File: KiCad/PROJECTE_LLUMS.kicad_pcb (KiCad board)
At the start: 2 copper layers, 82.8 x 63 mm, 60 parts, among them J1 CONNECTOR_MOTOR, J2 Conn_01x03, J3 Conn_01x03, Q2 IRLZ44N, Q3 IRLZ44N, Q4 IRLZ44N, Q5 IRLZ44N, Q6 IRLZ44N, Q7 IRLZ44N, SW1 SW_Push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

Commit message: routing
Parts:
- added C10: 10uF, Capacitor_SMD:C_0805_2012Metric_Pad1.18x1.45mm_HandSolder, F.Cu at (92.6, 109.4)
- added C11: 10uF, Capacitor_SMD:C_0805_2012Metric_Pad1.18x1.45mm_HandSolder, F.Cu at (89.7, 109.3)
- added J4: Conn_01x02_Pin, TerminalBlock:TerminalBlock_MaiXu_MX126-5.0-02P_1x02_P5.00mm, F.Cu at (102.5, 76.9)
- moved D6 311.5 mm to (240.8, 80.9), turned to 180 degrees
- moved D5 307.6 mm to (240.8, 88.3), turned to 180 degrees
- moved D4 304.3 mm to (240.8, 95.8), turned to 180 degrees
- moved D3 301.8 mm to (240.8, 103.3), turned to 180 degrees
- moved D2 300.0 mm to (240.8, 110.7), turned to 180 degrees
- moved Q7 295.7 mm to (232.6, 80.8), turned to 180 degrees
- moved R2 294.1 mm to (238.5, 120.2), turned to 180 degrees
- moved Q6 292.4 mm to (232.6, 86.8), turned to 180 degrees
- moved Q5 289.5 mm to (232.6, 92.7), turned to 180 degrees
- moved Q4 287.0 mm to (232.6, 98.7), turned to 180 degrees
- moved Q3 285.1 mm to (232.6, 104.6), turned to 180 degrees
- moved Q2 283.6 mm to (232.6, 110.5), turned to 180 degrees
- moved R3 275.0 mm to (229.0, 120.2), turned to 180 degrees
- moved J1 262.4 mm to (220.8, 103.0), turned to 180 degrees
- moved D7 262.2 mm to (221.9, 111.1), turned to 180 degrees
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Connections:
- net 12V renamed /alimentacio/12V
- net Net-(D8-A) renamed /alimentacio/OUT
- net Net-(J3-Pin_1) renamed /Debug/CON1
- net Net-(J3-Pin_2) renamed /Debug/CON2
- net Net-(U7-OSC1/CLKI/CN30/RA2) renamed /microcontrolador/OSC1
- net Net-(U7-OSC2/CLKO/CN29/PMA0/RA3) renamed /microcontrolador/OSC2
- net Net-(U7-VCAP) renamed /microcontrolador/VCAP
- net Net-(U7-~{MCLR}) renamed /microcontrolador//MCLR
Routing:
- net VSS: track 0.00 -> 110.1 mm, vias 0 -> 53
- net 5V: track 0.00 -> 81.4 mm
- net /alimentacio/OUT: track 0.00 -> 13.3 mm
- net /alimentacio/12V: track 0.00 -> 13.2 mm
- added copper zone on F.Cu, net 3V3
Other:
- board size 82.8 x 63 mm -> 94.8 x 53.8 mm
- board text added: "PROBABLEMENT S'HAGI DE CANVIAR EL CONNECTOR J4"

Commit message: DRC
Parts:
- moved R10 3.95 mm to (163.9, 76.8)
- moved R11 3.95 mm to (163.9, 85.3)
- moved R12 3.95 mm to (163.9, 93.8)
- moved R7 3.95 mm to (163.9, 119.5)
- moved R8 3.95 mm to (163.9, 110.9)
- moved R9 3.95 mm to (163.9, 102.5)
- moved REF** 3.95 mm to (178.6, 120.2)
- moved REF** 3.95 mm to (178.6, 73.2)
- moved SW1 3.95 mm to (173.5, 120.5)
- moved SW2 3.95 mm to (173.5, 112.0)
- moved SW3 3.95 mm to (173.5, 103.4)
- moved SW4 3.95 mm to (173.5, 77.7)
- moved SW5 3.95 mm to (173.5, 86.3)
- moved SW6 3.95 mm to (173.5, 94.9)
- moved C1 0.38 mm to (112.8, 92.9)
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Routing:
- net I2C_SDA: track 0.00 -> 34.7 mm
- net I2C_SCL: track 0.00 -> 27.7 mm
- net UART_RX: track 0.00 -> 19.3 mm
- net CANTX: track 0.00 -> 14.3 mm, vias 0 -> 2
- net BUS_CANL: track 0.00 -> 10.0 mm
- net /microcontrolador/OSC1: track 0.00 -> 9.77 mm
- net BUS_CANH: track 0.00 -> 9.65 mm
- net /microcontrolador/OSC2: track 0.00 -> 9.62 mm
- net UART_TX: track 0.00 -> 7.39 mm, vias 0 -> 2
- net /microcontrolador//MCLR: track 0.00 -> 4.29 mm
- net /Debug/CON1: track 0.00 -> 3.50 mm
- net /Debug/CON2: track 0.00 -> 3.48 mm
- net Net-(U4-VDD): track 0.00 -> 3.20 mm
- net CANRX: track 0.00 -> 2.92 mm
- net VSS: track 110.1 -> 110.0 mm, vias 53 -> 54
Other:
- board size 94.8 x 53.8 mm -> 98.8 x 53.8 mm

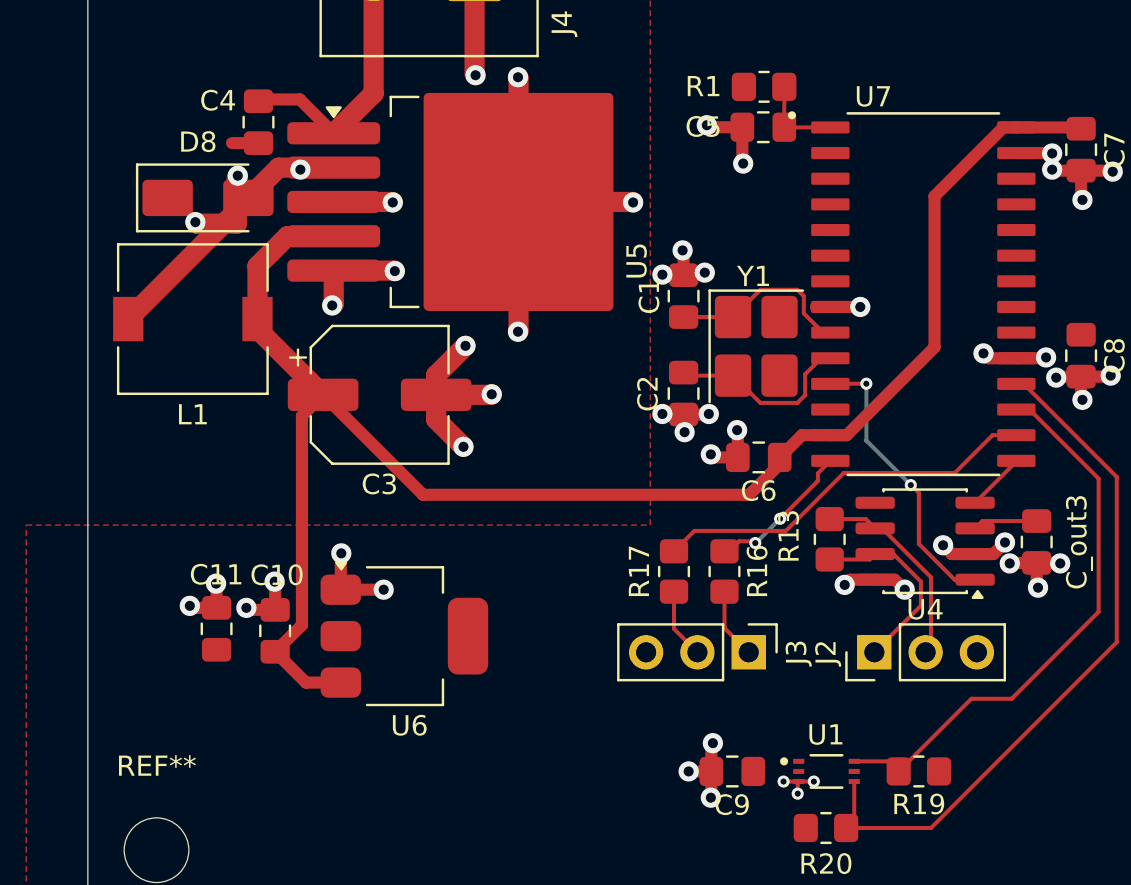
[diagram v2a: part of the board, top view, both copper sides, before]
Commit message: correcció d'errors CADLAB, falten els de llums i un parell que no entenc
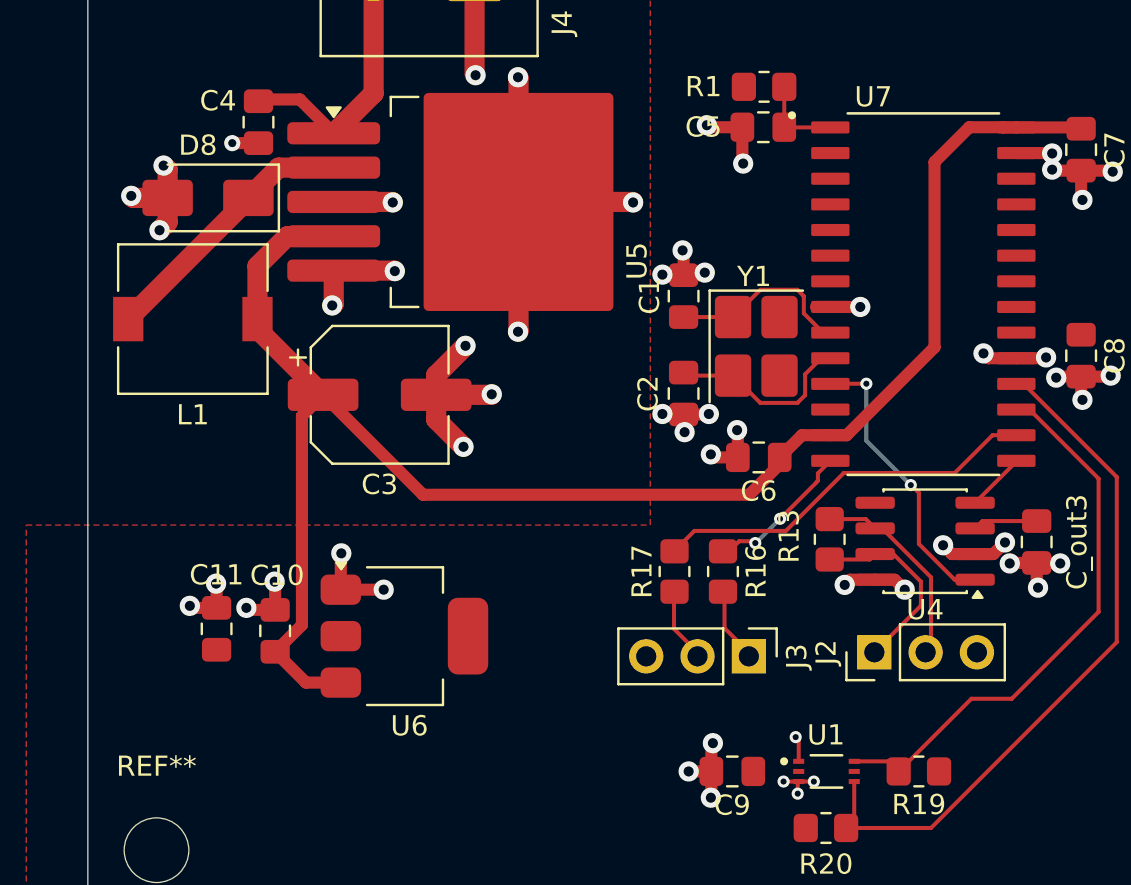
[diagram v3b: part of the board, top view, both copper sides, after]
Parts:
- C3: value 100uF -> 220uF
- C4: value 100nF -> 680uF
- moved J3 0.20 mm to (116.1, 110.7)
- moved R16 0.08 mm to (114.8, 106.5)
- turned D8 to 180 degrees
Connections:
- net /Debug/CON1 renamed /microcontrolador/CON1
- net /Debug/CON2 renamed /microcontrolador/CON2
- D8 pad 1: VSS -> /alimentacio/OUT
- D8 pad 2: /alimentacio/OUT -> VSS
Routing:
- net 3V3: track 0.00 -> 1.26 mm, vias 0 -> 1
- net 5V: track 81.4 -> 82.4 mm
- net VSS: track 110.0 -> 110.8 mm, vias 54 -> 55

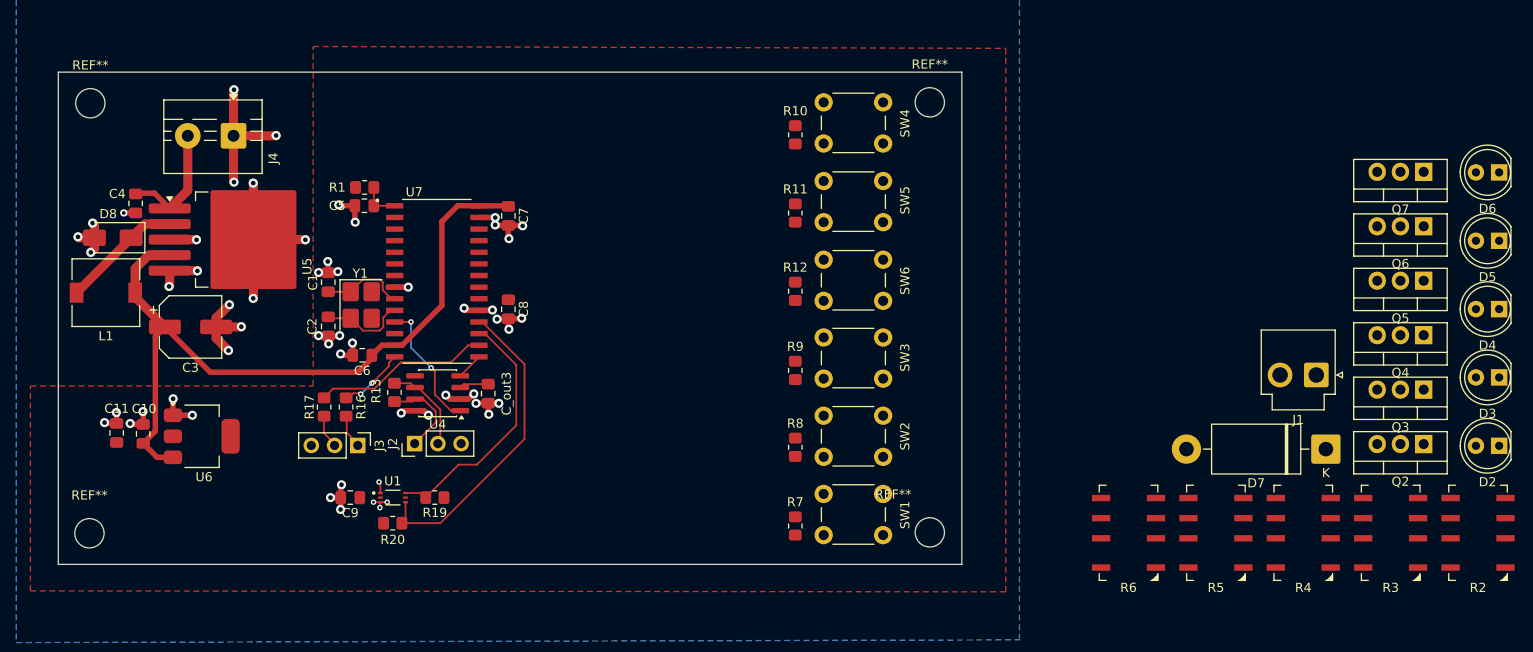
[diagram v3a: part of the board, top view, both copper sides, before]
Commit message: Esquemàtic acabat amb llums incorporades
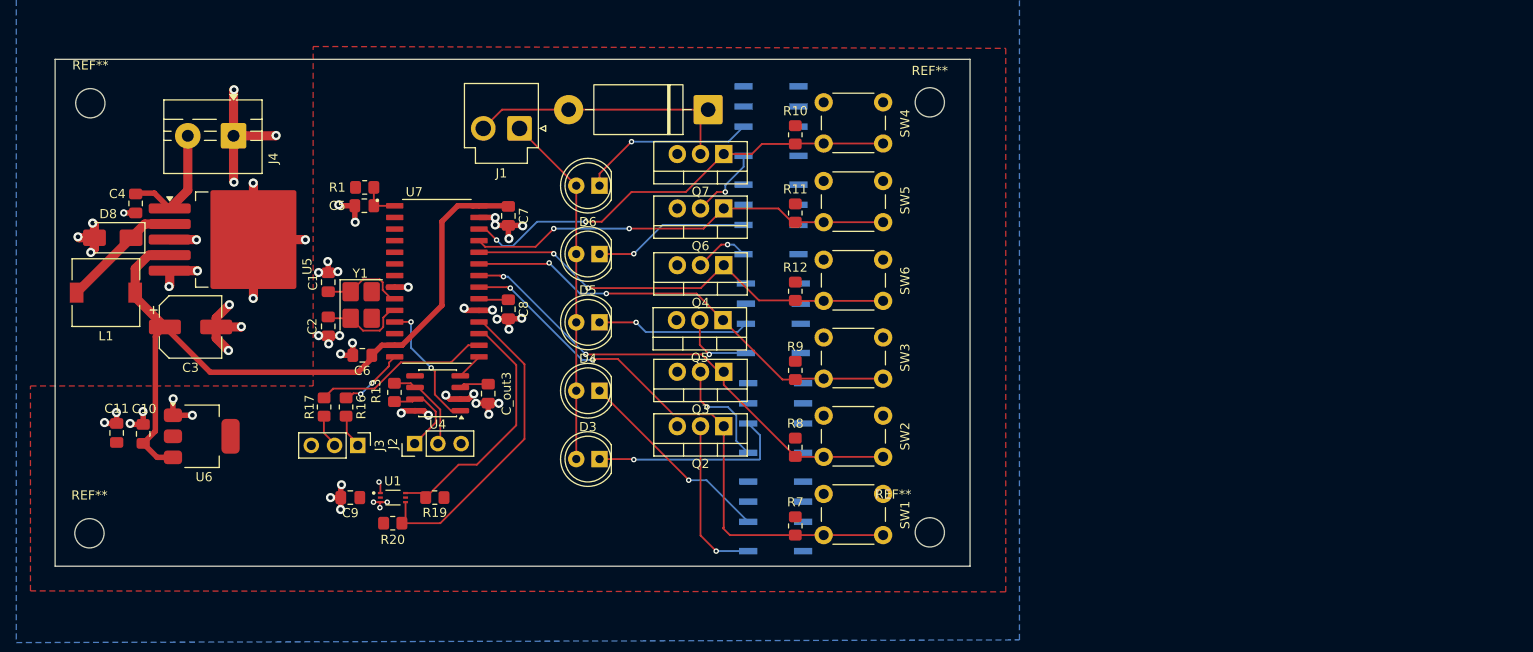
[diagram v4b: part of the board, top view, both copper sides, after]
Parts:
- R2, R3, R4, R5, R6: moved to B.Cu
- moved D2 98.3 mm to (142.5, 112.2)
- moved D3 98.3 mm to (142.5, 104.7)
- moved D4 98.3 mm to (142.5, 97.2)
- moved D5 98.3 mm to (142.5, 89.8)
- moved D6 98.3 mm to (142.5, 82.3)
- moved J1 91.2 mm to (133.8, 76.0)
- moved R2 77.8 mm to (161.8, 107.7), turned to 0 degrees
- moved D7 77.0 mm to (154.4, 74.0)
- moved Q4 76.9 mm to (156.1, 91.0)
- moved Q5 76.7 mm to (156.0, 97.0)
- moved Q2 76.5 mm to (156.1, 108.6)
- moved Q3 76.5 mm to (156.1, 102.7)
- moved Q6 76.5 mm to (156.1, 84.8)
- moved Q7 76.5 mm to (156.1, 78.8)
- moved R3 67.2 mm to (161.8, 118.5), turned to 0 degrees
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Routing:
- net CARRETERA: track 0.00 -> 62.1 mm, vias 0 -> 2
- net ENCREUAMENT: track 0.00 -> 53.2 mm, vias 0 -> 2
- net NETEJA-FARS: track 0.00 -> 49.6 mm, vias 0 -> 2
- net DIURNA: track 0.00 -> 49.5 mm, vias 0 -> 2
- net INTERM. ESQ: track 0.00 -> 48.4 mm, vias 0 -> 2
- net INTERM. DRT: track 0.00 -> 46.8 mm, vias 0 -> 2
- net +12V: track 0.00 -> 38.7 mm
- net Net-(D7-A): track 0.00 -> 30.6 mm
- net Net-(D3-K): track 0.00 -> 22.2 mm, vias 0 -> 1
- net Net-(D2-K): track 0.00 -> 22.0 mm, vias 0 -> 1
- net Net-(D6-K): track 0.00 -> 19.2 mm, vias 0 -> 1
- net Net-(Q2-D): track 0.00 -> 17.9 mm, vias 0 -> 1
- net Net-(D5-K): track 0.00 -> 17.1 mm, vias 0 -> 1
- net Net-(D4-K): track 0.00 -> 16.8 mm, vias 0 -> 1
- net Net-(Q3-D): track 0.00 -> 12.3 mm, vias 0 -> 1
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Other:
- board size 98.8 x 53.8 mm -> 100 x 55.4 mm

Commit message: errors pcb
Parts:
- removed J2: Conn_01x03, Connector_PinHeader_2.54mm:PinHeader_1x03_P2.54mm_Vertical
- added J5: DE9_Pins, Connector_Dsub:DSUB-9_Pins_Vertical_P2.77x2.84mm, F.Cu at (103.2, 164.1)
- added R14: 4.7k, Resistor_SMD:R_0805_2012Metric_Pad1.20x1.40mm_HandSolder, F.Cu at (120.9, 113.9)
- added R15: 10k, Resistor_SMD:R_0805_2012Metric_Pad1.20x1.40mm_HandSolder, F.Cu at (127.5, 109.5)
- moved R20 0.10 mm to (120.0, 119.2)
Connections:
- net BUS_CANH renamed /transciever/CANH
- net BUS_CANL renamed /transciever/CANL
- C1 pad 2: VSS -> GND
- C10 pad 2: VSS -> GND
- C11 pad 2: VSS -> GND
- C2 pad 2: VSS -> GND
- C3 pad 2: VSS -> GND
- C4 pad 2: VSS -> GND
- C5 pad 2: VSS -> GND
- C6 pad 2: VSS -> GND
- C7 pad 2: VSS -> GND
- C8 pad 2: VSS -> GND
- C9 pad 2: VSS -> GND
- C_out3 pad 1: VSS -> GND
- D8 pad 2: VSS -> GND
- J3 pad 3: VSS -> GND
- J4 pad 1: VSS -> GND
- Q2 pad 3: VSS -> GND
- Q3 pad 3: VSS -> GND
- Q4 pad 3: VSS -> GND
- Q5 pad 3: VSS -> GND
- Q6 pad 3: VSS -> GND
- Q7 pad 3: VSS -> GND
- R19 pad 1: 3V3 -> /sensor_llum/SCL
- R19 pad 2: I2C_SCL -> 3V3
- SW1 pad 2: VSS -> GND
- SW2 pad 2: VSS -> GND
- SW3 pad 2: VSS -> GND
- SW4 pad 2: VSS -> GND
- SW5 pad 2: VSS -> GND
- SW6 pad 2: VSS -> GND
- U1 pad 2: VSS -> GND
- U1 pad 3: VSS -> GND
- U1 pad 4: I2C_SDA -> /sensor_llum/SDA
- U1 pad 6: I2C_SCL -> /sensor_llum/SCL
- U4 pad 2: VSS -> GND
- U4 pad 8: VSS -> /transciever/Rs
- U5 pad 3: VSS -> GND
- U5 pad 5: VSS -> GND
- U6 pad 1: VSS -> GND
- U7 pad 17: I2C_SCL -> 3V3
- U7 pad 18: I2C_SDA -> 3V3
- U7 pad 19: VSS -> GND
- U7 pad 27: VSS -> GND
- U7 pad 8: VSS -> GND
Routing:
- net GND: track 0.00 -> 111.4 mm, vias 0 -> 56
- net VSS: track 110.8 -> 0.00 mm, vias 55 -> 0
- net 3V3: track 1.26 -> 30.4 mm
- net I2C_SCL: track 27.7 -> 0.00 mm
- net /transciever/CANL: track 10.0 -> 2.79 mm
- net /sensor_llum/SCL: track 0.00 -> 6.45 mm
- net /transciever/CANH: track 9.65 -> 3.26 mm
- net /transciever/Rs: track 0.00 -> 5.24 mm
- net /sensor_llum/SDA: track 0.00 -> 3.87 mm
- net I2C_SDA: track 34.7 -> 32.8 mm
- added copper zone on B.Cu, net GND
- removed copper zone on B.Cu, net VSS
